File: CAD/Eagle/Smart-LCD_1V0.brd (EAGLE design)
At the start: 99 x 74.5 mm, 27 parts, among them Q1 BC337-40, U101 MEGA32-P, U221 MCP4018T-104E/LT, X201 LCD_23WAY__UC1608, X301 I2C

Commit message: CAD - first layout worked on
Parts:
- removed Q1: BC337-40, df4iah_bipoltransistor:TO92
- removed TP1, TP2: TPPAD1-20, df4iah_connector:P1-20
- added C131: 100pF, rcl:C0805
- added LED_A, LED_K: TPPAD1-20, df4iah_connector:P1-20
- added Q121: MMBT2222AL, df4iah_bipoltransistor:SOT23
- added R131: 33kR, rcl:R0805
- added X131: LDR, df4iah_connector:1X02
- R121: value 52kR -> 18kR
- R391, R392: value (none) -> 1.5kR
- moved R121 185.8 mm to (33.0, 53.3), flipped to the bottom, turned to 90 degrees
- moved R101 185.2 mm to (47.0, 54.6), flipped to the bottom, turned to 180 degrees
- moved C301 178.0 mm to (71.1, 61.0), flipped to the bottom, turned to 270 degrees
- moved C302 173.3 mm to (63.5, 66.0), flipped to the bottom
- moved C101 171.9 mm to (49.5, 52.1), flipped to the bottom, turned to 180 degrees
- moved C111 154.1 mm to (45.7, 27.9), flipped to the bottom, turned to 270 degrees
- moved C102 145.4 mm to (49.5, 29.2), flipped to the bottom
- moved U221 135.5 mm to (72.4, 25.4), flipped to the bottom, turned to 180 degrees
- moved R222 121.3 mm to (72.4, 22.9), flipped to the bottom
- moved C221 102.7 mm to (41.9, 12.1), flipped to the bottom
- moved R221 95.8 mm to (43.2, 8.89), flipped to the bottom, turned to 270 degrees
- moved R211 84.5 mm to (40.6, 8.89), flipped to the bottom, turned to 270 degrees
- moved C211 76.6 mm to (41.9, 2.54), flipped to the bottom, turned to 180 degrees
- moved C202 73.3 mm to (37.5, 8.89), flipped to the bottom, turned to 270 degrees
- moved C201 66.7 mm to (34.3, 8.89), flipped to the bottom, turned to 270 degrees
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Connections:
- net N$1 renamed AREF
- net N$2 renamed POT_A
- removed net LED_A: Q1.1, TP1.TP
- removed net VDD: R222.2, U221.1, X201.8
- removed net VSS: C211.2, C221.2, R211.1, TP2.TP, U221.2, X201.7
- new net LDR: C131.1, U101.40, X131.2
- new net LDR_P: R131.2, X131.1
- new net LED_K: LED_K.TP, Q121.3
- net !RST: now also U101.5
- net +3V3: now also R131.1, R222.2, U221.1, X201.8; no longer Q1.3
- net +5V: now also LED_A.TP
- net BM0: now also U101.2
- net BM1: now also U101.1
- net CD: now also U101.6
- net CS: now also U101.3
- net D0: now also U101.14
- net D1: now also U101.15
- net D2: now also U101.16
- net D3: now also U101.17
- net D4: now also U101.18
- net D5: now also U101.19
- net D6: now also U101.20
- net D7: now also U101.21
- net GND: now also C131.2, C211.2, C221.2, Q121.2, R211.1, U221.2, X201.7
- net LED_PWM_B: now also Q121.1; no longer Q1.2
- net VBIAS: now also R221.2
- net WR0: now also U101.7
- net WR1: now also U101.8
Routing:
- net BM1: track 0.00 -> 151.2 mm
- net BM0: track 0.00 -> 147.8 mm
- net CS: track 0.00 -> 144.4 mm
- net !RST: track 0.00 -> 138.4 mm
- net CD: track 0.00 -> 134.9 mm
- net WR0: track 0.00 -> 131.5 mm
- net +3V3: track 0.00 -> 129.7 mm
- net WR1: track 0.00 -> 128.1 mm
- net D0: track 0.00 -> 111.9 mm
- net +5V: track 0.00 -> 111.6 mm, vias 0 -> 1
- net LED_PWM_B: track 0.00 -> 111.1 mm
- net D1: track 0.00 -> 108.5 mm
- net D2: track 0.00 -> 105.0 mm
- net D3: track 0.00 -> 101.6 mm
- net D4: track 0.00 -> 98.2 mm
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- added copper zone on layer 1, net GND
- added copper zone on layer 16, net GND
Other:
- board text added: "LDR"

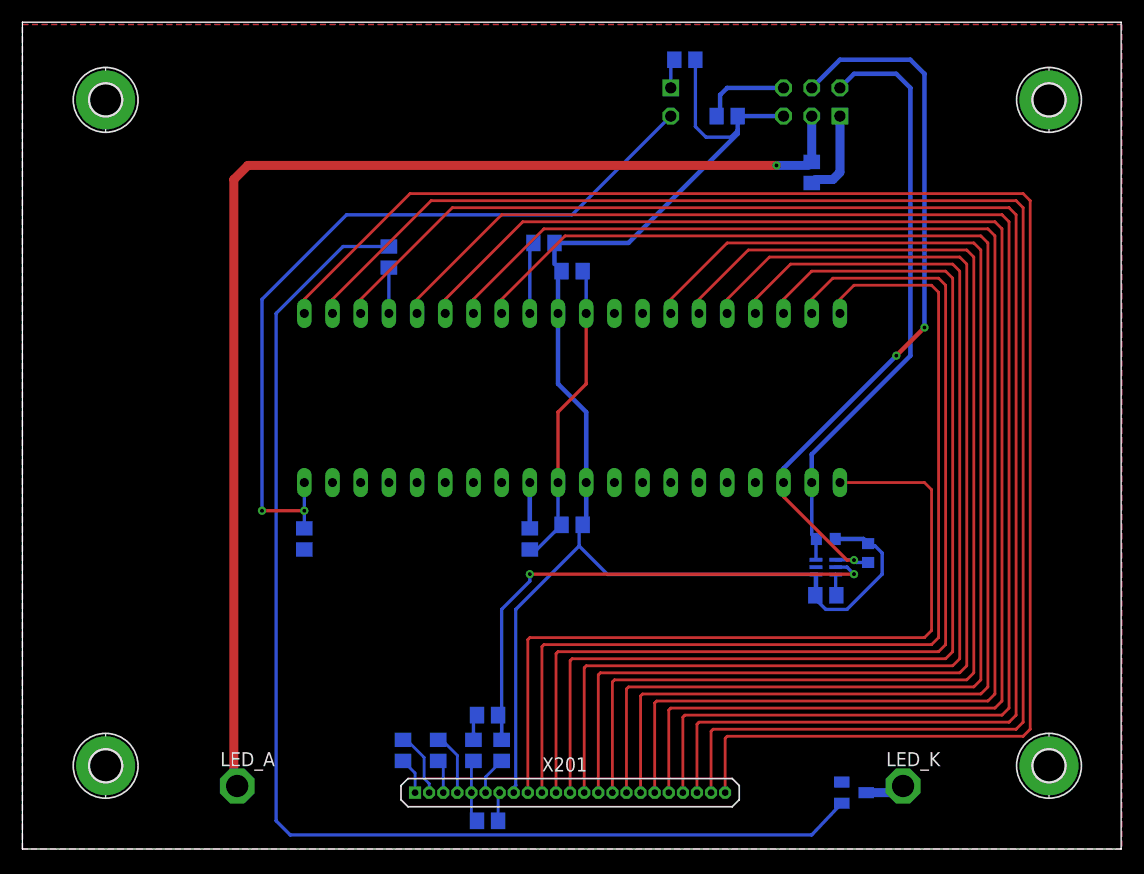
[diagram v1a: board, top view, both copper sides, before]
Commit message: CAD - routed, but audio amplifier still TODO
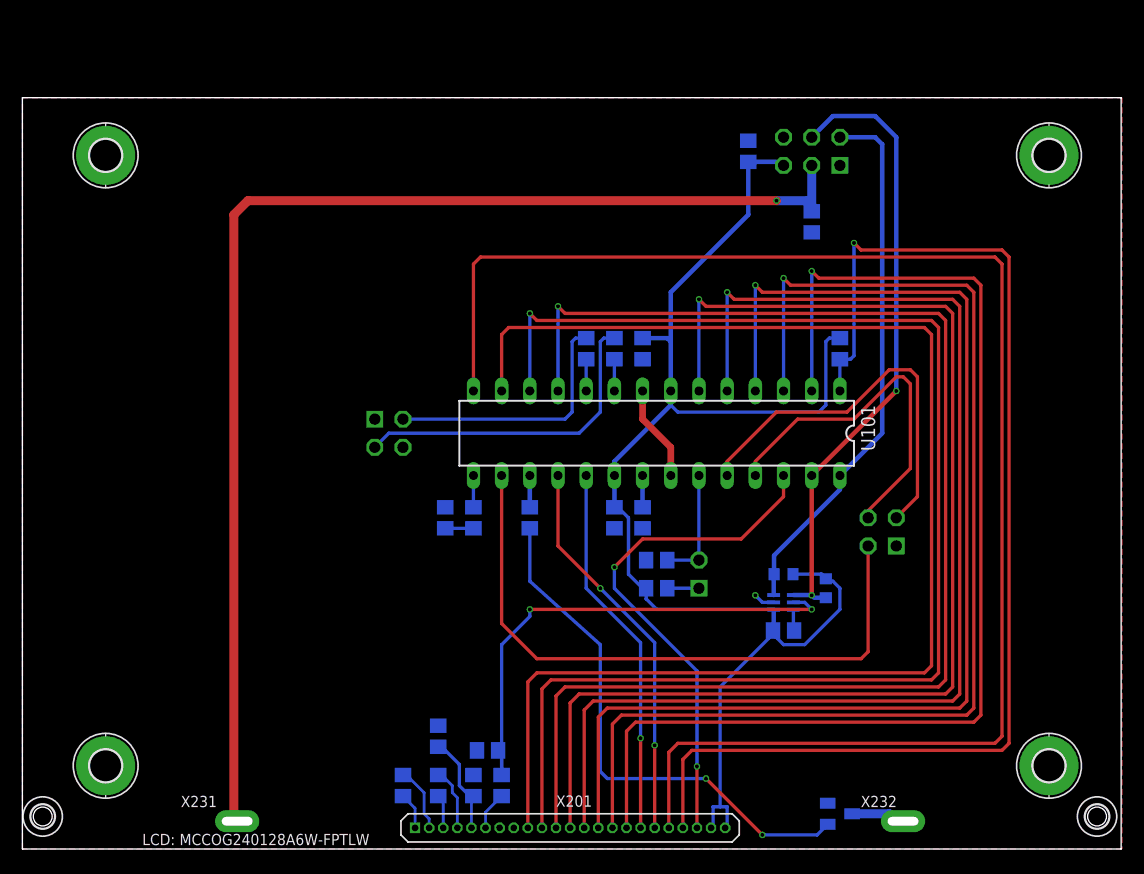
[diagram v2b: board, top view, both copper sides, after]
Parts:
- removed LED_A, LED_K: TPPAD1-20, df4iah_connector:P1-20
- added C141: 100pF, rcl:C0805
- added H411, H412: MOUNT-HOLE1.7, df4iah_holes:1,7
- added R141: 18kR, rcl:R0805
- added R151, R152: 330R, rcl:R0805
- added X141: Switches, df4iah_connector:2X02
- added X151: LEDs, df4iah_connector:2X02
- added X231: LED_A, df4iah_connector:P1-20X0.80
- added X232: LED_K, df4iah_connector:P1-20X0.80
- U101: value MEGA32-P -> MEGA8-P; device df4iah_processors:DIL40 -> df4iah_processors:DIL28-3
- moved R131 47.7 mm to (57.1, 23.5), turned to 180 degrees
- moved X131 45.2 mm to (61.0, 23.5), turned to 0 degrees
- moved C131 31.8 mm to (57.1, 26.0), turned to 0 degrees
- moved R101 28.3 mm to (73.7, 45.1), turned to 270 degrees
- moved R121 26.7 mm to (45.7, 29.8), turned to 270 degrees
- moved C111 10.3 mm to (55.9, 29.8), turned to 90 degrees
- moved C101 9.44 mm to (55.9, 45.1), turned to 270 degrees
- moved C211 8.82 mm to (37.5, 10.2), turned to 90 degrees
- moved U101 8.25 mm to (57.1, 37.5), flipped to the top
- moved H401 5.00 mm to (7.50, 62.5)
- moved H403 5.00 mm to (92.5, 62.5)
- moved R222 4.96 mm to (68.6, 19.7)
- moved R391 4.96 mm to (68.6, 24.8)
- moved R392 4.96 mm to (72.4, 23.5)
- moved U221 4.96 mm to (68.6, 22.2)
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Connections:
- removed net !RESET: R101.1, U101.9
- removed net BM0: U101.2, X201.22
- removed net BM1: U101.1, X201.23
- new net AG: R152.1, X151.3
- new net AG_D: R152.2, U101.10
- new net AR: R151.1, X151.2
- new net AR_D: R151.2, U101.9
- new net AUDIO_D: R141.1, U101.15
- new net AUDIO_LP: C141.1, R141.2
- new net SW_I: U101.24, X141.2
- new net SW_P: U101.16, X141.3
- new net SW_Q: U101.25, X141.4
- net !RST: now also R101.2, U101.1; no longer U101.5
- net +3V3: now also R101.1, U101.20, U101.7, X201.22, X201.23; no longer R101.2, U101.10, U101.30
- net +5V: now also X231.1; no longer LED_A.TP
- net AREF: now also C111.2, U101.21; no longer C111.1, U101.32
- net CD: now also U101.14; no longer U101.6
- net CS: now also U101.26; no longer U101.3
- net D0: now also U101.2; no longer U101.14
- net D1: now also U101.3; no longer U101.15
- net D2: now also U101.4; no longer U101.16
- net D3: now also U101.5; no longer U101.17
- net D4: now also U101.6; no longer U101.18
- net D5: now also U101.11; no longer U101.19
- net D6: now also U101.12; no longer U101.20
- net D7: now also U101.13; no longer U101.21
- net GND: now also C111.1, C141.2, U101.22, U101.8, X141.1, X151.1; no longer C111.2, U101.11, U101.31
- net LDR: now also U101.23; no longer U101.40
- net LED_K: now also X232.1; no longer LED_K.TP
- net LED_PWM_D: now also U101.17; no longer U101.4
- net SCL: now also U101.28; no longer U101.22
- net SDA: now also U101.27; no longer U101.23
- net WR0: now also U101.18; no longer U101.7
- net WR1: now also U101.19; no longer U101.8
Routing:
- net BM1: track 151.2 -> 0.00 mm
- net BM0: track 147.8 -> 0.00 mm
- net CS: track 144.4 -> 46.4 mm, vias 0 -> 2
- net WR0: track 131.5 -> 35.4 mm, vias 0 -> 2
- net WR1: track 128.1 -> 33.8 mm, vias 0 -> 1
- net LED_PWM_B: track 111.1 -> 48.0 mm, vias 0 -> 2
- net LDR: track 70.7 -> 10.5 mm, vias 2 -> 0
- net SW_P: track 0.00 -> 57.5 mm
- net D7: track 71.7 -> 124.3 mm
- net GND: track 48.9 -> 11.2 mm, vias 0 -> 1
- net SW_I: track 0.00 -> 35.6 mm
- net D6: track 91.3 -> 124.3 mm, vias 0 -> 1
- net SW_Q: track 0.00 -> 32.3 mm
- net !RST: track 138.4 -> 108.9 mm, vias 0 -> 1
- net AR: track 0.00 -> 29.4 mm
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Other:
- board size 99 x 74.5 mm -> 99 x 67.7 mm
- board text added: "I2C"
- board text added: "LCD: MCCOG240128A6W-FPTLW"
- board text added: "LEDs"
- board text added: "Switches"

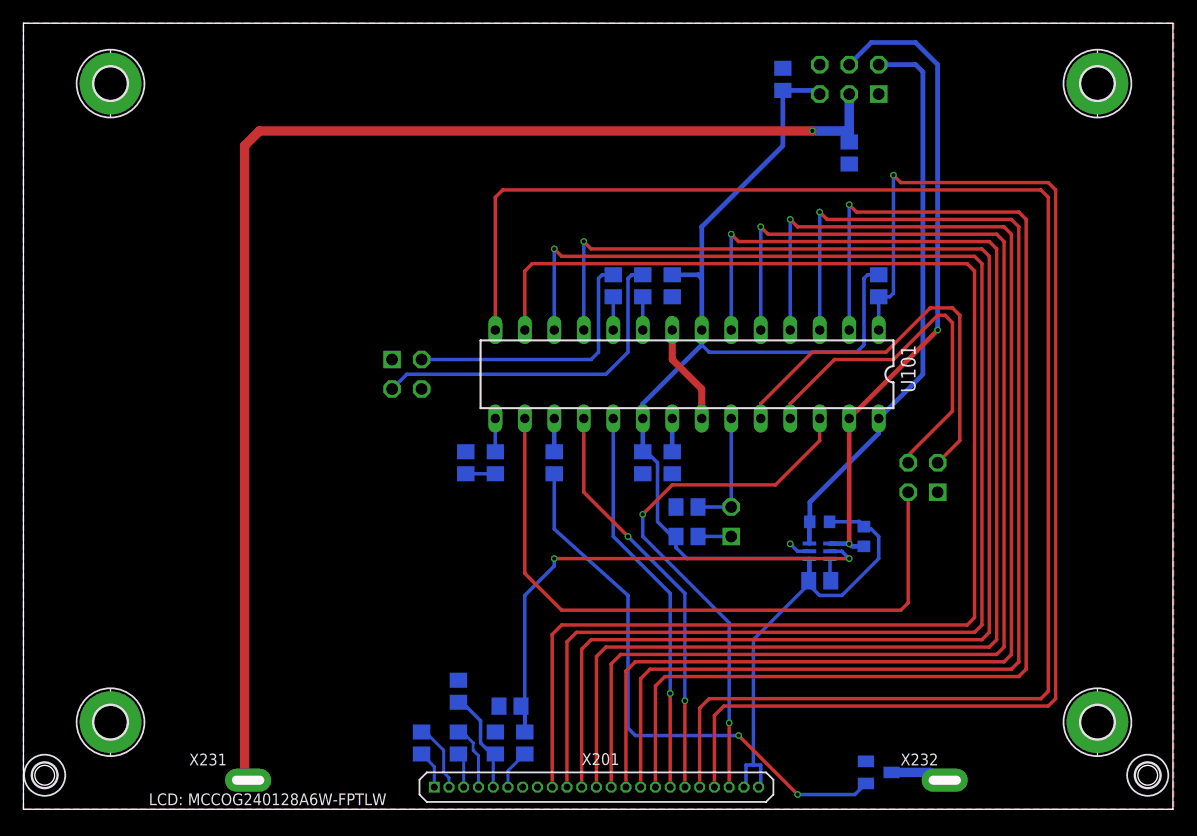
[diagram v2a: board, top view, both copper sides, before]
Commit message: CAD - audio amplifier added, but CPU must be placed on the solder side
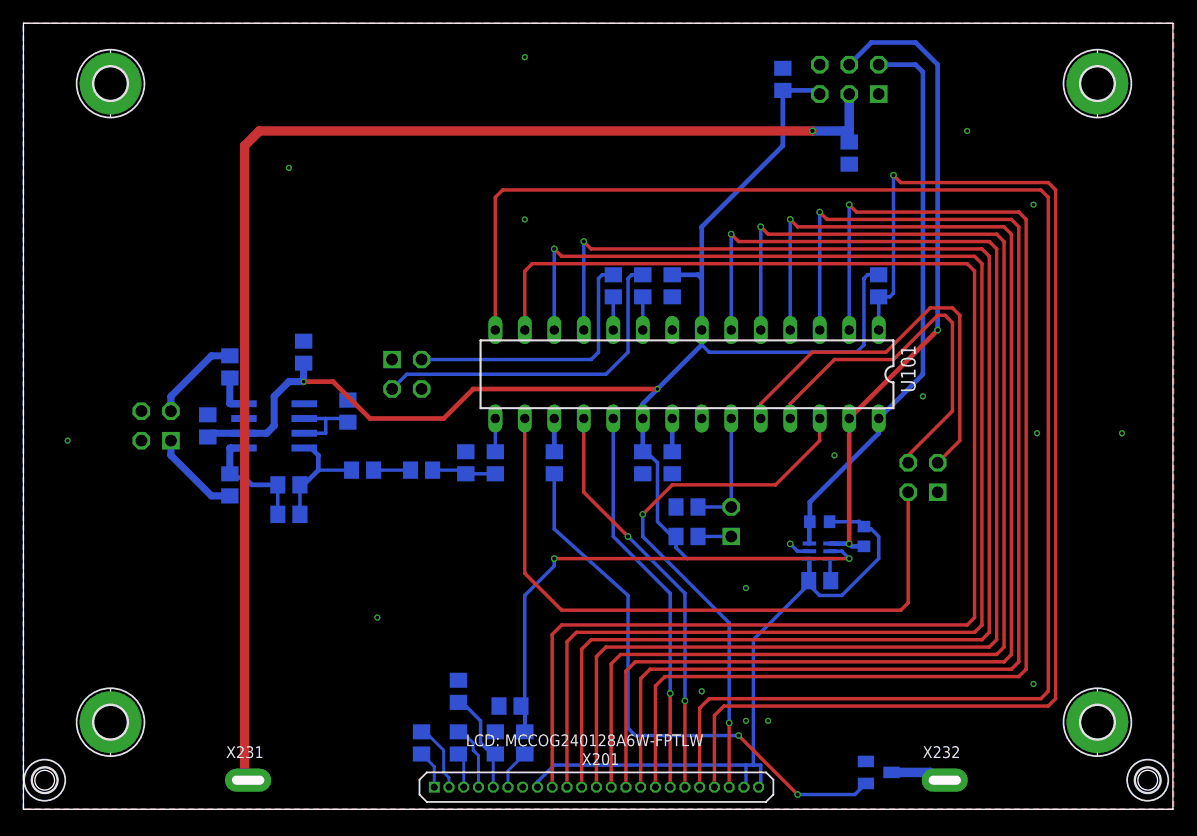
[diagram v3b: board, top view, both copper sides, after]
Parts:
- removed C141: 100pF, rcl:C0805
- removed H411, H412: MOUNT-HOLE1.7, df4iah_holes:1,7
- added C103: 100pF, rcl:C0805
- added C401: 22uF, rcl:C0805
- added C402: 100nF, rcl:C0805
- added C411, C412: 47uF, rcl:C0805
- added C431: 1uF, rcl:C0805
- added C452: 470pF, rcl:C0805
- added C455: 470nF, rcl:C0805
- added H511, H512: MOUNT-HOLE1.7, df4iah_holes:1,7
- added R451, R454: 22kR, rcl:R0805
- added U401: TS4871ID, df4iah_opamp:SO08
- added X411: Audio, df4iah_connector:2X02
- C111: value 100pF -> 22nF
- R111: value 18kR -> 3.3kR
- moved C111 17.8 mm to (38.1, 29.8)
- renumbered H401 to H502, H402 to H501, H403 to H504, H404 to H503, R141 to R111
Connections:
- new net AU454: C455.1, R454.2
- new net BYPASS: C431.1, U401.2, U401.3
- new net SPK_N: C412.2, X411.2
- new net SPK_P: C411.2, X411.1
- new net VIN_N: C452.1, C455.2, R451.1, U401.4
- new net VOUT1: C411.1, C452.2, R451.2, U401.5
- new net VOUT2: C412.1, U401.8
- net +3V3: now also C401.1, C402.1, U401.6
- net AREF: now also C103.2; no longer C111.2
- net AUDIO_LP: now also C111.1, R454.1; no longer C141.1
- net GND: now also C103.1, C111.2, C401.2, C402.2, C431.2, U401.1, U401.7; no longer C111.1, C141.2
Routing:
- net +3V3: track 125.5 -> 190.7 mm, vias 0 -> 2
- net VOUT1: track 0.00 -> 10.5 mm
- net VIN_N: track 0.00 -> 10.3 mm
- net GND: track 11.2 -> 2.56 mm, vias 1 -> 17
- net SPK_P: track 0.00 -> 7.80 mm
- net SPK_N: track 0.00 -> 7.80 mm
- net BYPASS: track 0.00 -> 7.00 mm
- net VOUT2: track 0.00 -> 3.43 mm
- net AU454: track 0.00 -> 3.18 mm
- net AUDIO_LP: track 2.54 -> 5.53 mm
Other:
- board text added: "Audio"

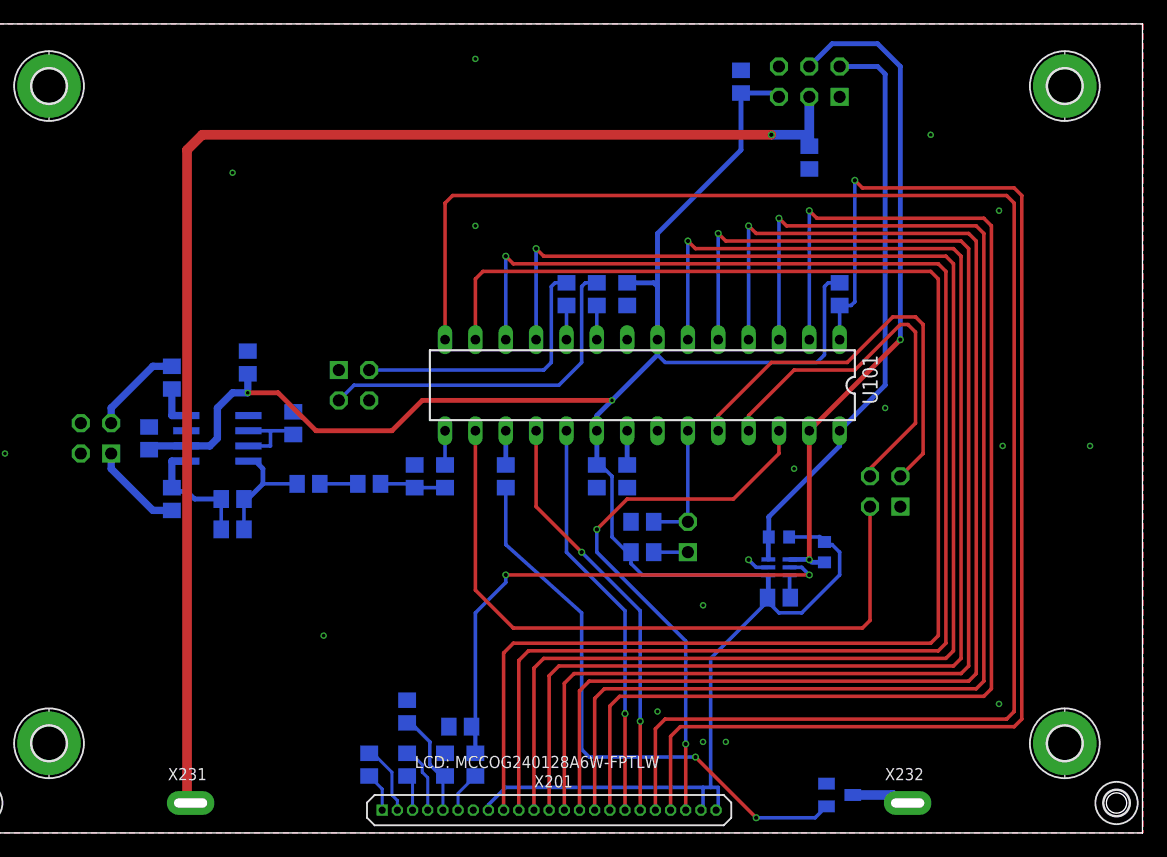
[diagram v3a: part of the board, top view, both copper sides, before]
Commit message: CAD - CPU placed on the solder side
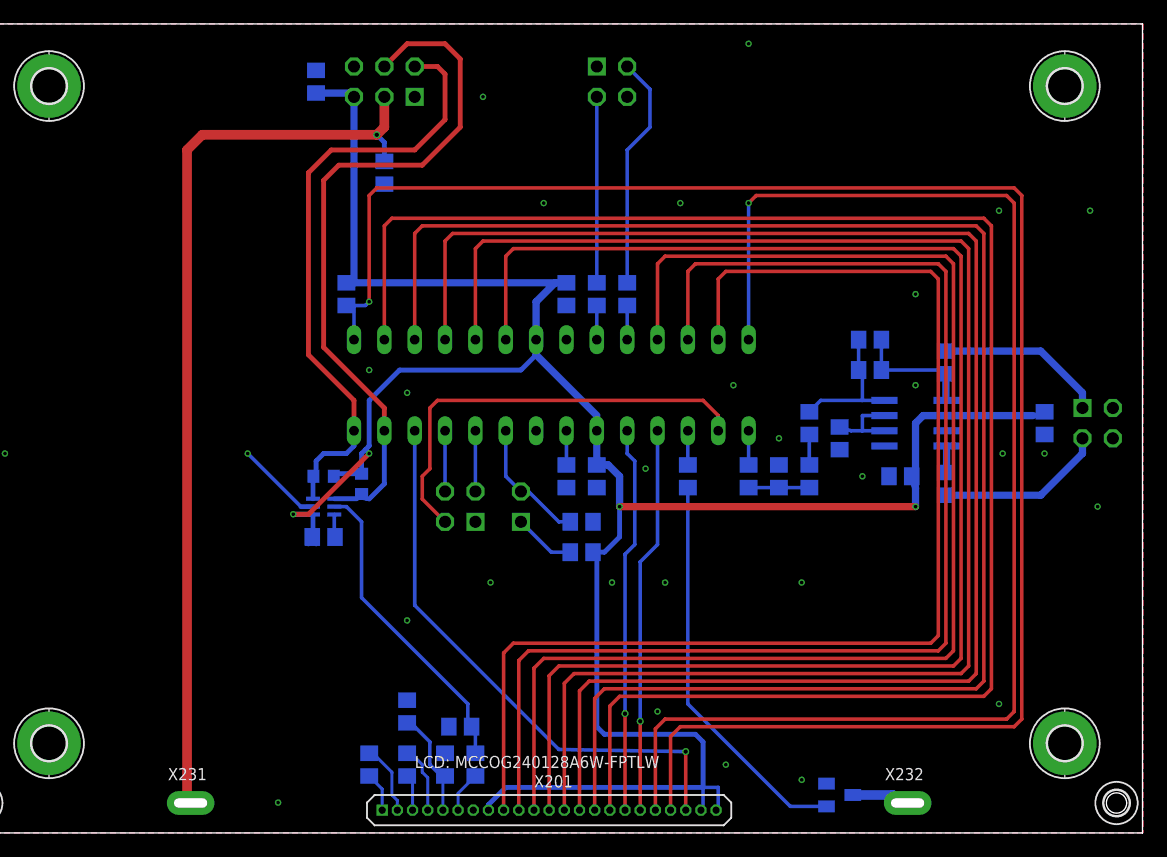
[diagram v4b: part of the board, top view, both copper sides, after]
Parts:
- moved X411 83.8 mm to (95.2, 34.3), turned to 180 degrees
- moved C402 74.9 mm to (90.8, 34.3), turned to 270 degrees
- moved C411 65.8 mm to (82.5, 39.4), turned to 90 degrees
- moved C412 65.4 mm to (82.5, 29.2), turned to 270 degrees
- moved U401 58.4 mm to (80.0, 34.3), turned to 90 degrees
- moved C452 55.7 mm to (76.2, 41.3), turned to 180 degrees
- moved C401 55.4 mm to (78.7, 29.8), turned to 0 degrees
- moved R451 54.4 mm to (76.2, 38.7), turned to 180 degrees
- moved C431 45.7 mm to (73.7, 33.0), turned to 270 degrees
- moved C455 42.2 mm to (71.1, 34.3), turned to 90 degrees
- moved R101 41.3 mm to (32.4, 45.1)
- moved R392 39.2 mm to (33.7, 29.2)
- moved R222 38.4 mm to (30.5, 24.8)
- moved R391 38.4 mm to (30.5, 29.8)
- moved U221 38.4 mm to (30.5, 27.3)
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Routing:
- net !RST: track 108.9 -> 148.9 mm
- net +5V: track 112.3 -> 77.1 mm
- net D0: track 106.5 -> 140.8 mm, vias 1 -> 0
- net SW_I: track 35.6 -> 5.08 mm
- net D1: track 107.8 -> 137.0 mm, vias 1 -> 0
- net SW_Q: track 32.3 -> 5.08 mm
- net CD: track 139.6 -> 114.2 mm, vias 0 -> 1
- net D2: track 109.1 -> 133.2 mm, vias 1 -> 0
- net SW_P: track 57.5 -> 36.8 mm
- net D7: track 124.3 -> 104.0 mm
- net POT_W: track 45.6 -> 26.1 mm, vias 2 -> 0
- net D3: track 110.3 -> 129.4 mm, vias 1 -> 0
- net D6: track 124.3 -> 107.8 mm, vias 1 -> 0
- net LED_PWM_B: track 48.0 -> 33.2 mm, vias 2 -> 0
- net D4: track 111.6 -> 125.6 mm, vias 1 -> 0
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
